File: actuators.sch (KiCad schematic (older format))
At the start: 16 parts

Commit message: Add digital outputs with NPN stage
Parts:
- added CONN? (x10): GPO, symbol GPO
- added Q? (x10): MBT3904DW1T1, SOT-363, symbol MBT3904DW1T1
- added R? (x10): 1k, symbol R_Small
- added R? (x10): 150, symbol R_Small
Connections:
- net labels added: OUT_1, OUT_10, OUT_2, OUT_3, OUT_4, OUT_5, OUT_6, OUT_7, OUT_8, OUT_9
- wire segments 28 -> 68
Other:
- note added: "150 ohm resistor limits NPN current to about 20mA"

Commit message: Annotate
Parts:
- gave numbers to parts that had none: 51

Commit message: Add connector for RGB LED
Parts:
- added CONN?: RGB, symbol RGB
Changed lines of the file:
@@
 Text Notes 1350 6150 0    60   ~ 0
 150 ohm resistor limits NPN current to about 20mA
+$Comp
+L RGB CONN?
+U 1 1 56BE642C
+P 10450 2325
+F 0 "CONN?" H 10627 2627 59  0000 L CNN
+F 1 "RGB" H 10627 2523 59  0000 L CNN
+F 2 "" H 10450 2325 59  0000 C CNN
+F 3 "" H 10450 2325 59  0000 C CNN
+	1    10450 2325
+	1    0    0    -1
+$EndComp
+Text Label 10100 1925 2    47   ~ 0
+RGB_LED_R
+Text Label 10100 2025 2    47   ~ 0
+RGB_LED_G
+Text Label 10100 2125 2    47   ~ 0
+RGB_LED_B
+$Comp
+L GND #PWR?
+U 1 1 56BE6827
+P 10100 2225
+F 0 "#PWR?" H 10100 1975 50  0001 C CNN
+F 1 "GND" H 10100 2075 50  0000 C CNN
+F 2 "" H 10100 2225 50  0000 C CNN
+F 3 "" H 10100 2225 50  0000 C CNN
+	1    10100 2225
+	1    0    0    -1
+$EndComp
 $EndSCHEMATC

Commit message: Correct digital outputs as we want to drive loads (LEDs)
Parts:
- removed CONN15, CONN16, CONN27, CONN28, CONN39, CONN40, CONN46, CONN47, CONN7, CONN8: GPO, symbol GPO
- added CONN15, CONN16, CONN27, CONN28, CONN39, CONN40, CONN46, CONN47, CONN7, CONN8: LOAD, symbol LOAD
- gave numbers to parts that had none: 1
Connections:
- wire segments 68 -> 77
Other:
- note added: "150 ohm resistor limits NPN current to \nabout 20mA if the load has no resistance"
- note removed: "150 ohm resistor limits NPN current to about 20mA"
- moved on the sheet: Q1B, Q2B, Q3B, Q4B, Q5B, R15, R2, R27, R3, R39, R49

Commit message: Fix small details & replot pdf
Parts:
- renumbered C1 to C17, CONN7 to CONN17, CONN8 to CONN18, CONN15 to CONN19, CONN16 to CONN20, CONN17 to CONN21, CONN18 to CONN22, CONN25 to CONN23, CONN26 to CONN24, CONN27 to CONN25, CONN28 to CONN26, CONN29 to CONN27, CONN30 to CONN28, CONN35 to CONN29, CONN36 to CONN30, CONN39 to CONN31, CONN40 to CONN32, CONN37 to CONN33, CONN38 to CONN34, CONN43 to CONN35, CONN44 to CONN36, CONN46 to CONN37, CONN47 to CONN38, CONN45 to CONN39, CONN54 to CONN40, R1 to R43, R2 to R44, R3 to R45, R4 to R46, R5 to R47, R14 to R48, R15 to R49, R16 to R50, R17 to R51, R26 to R52, R27 to R53, R28 to R54, R29 to R55, R38 to R56, R39 to R57, R44 to R58, R45 to R59, R48 to R60, R49 to R61, R50 to R62, R51 to R63, U1 to U6

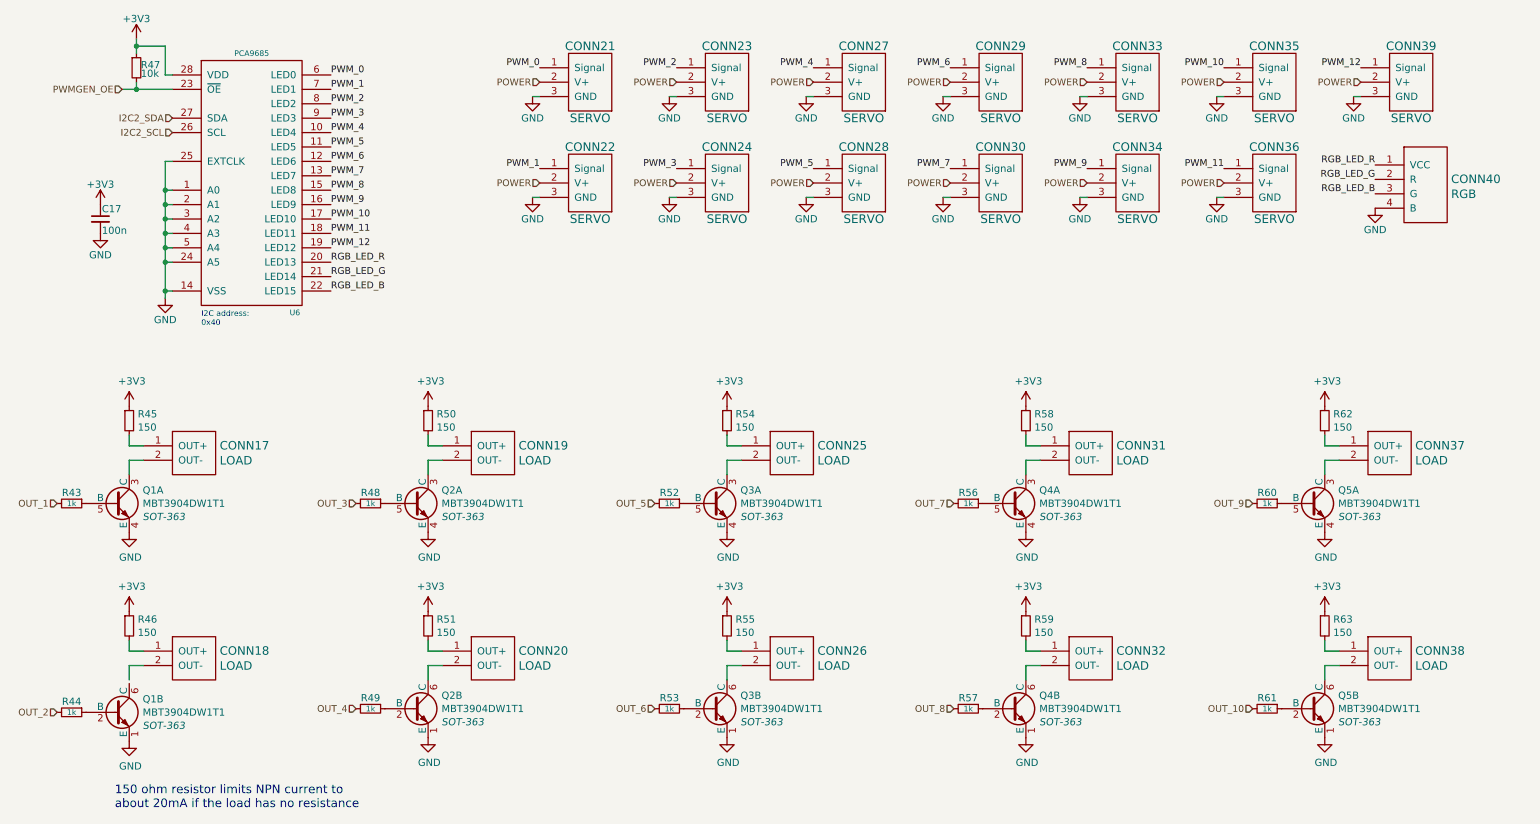
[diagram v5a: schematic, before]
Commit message: Correct schematic after review by @vieillemaison
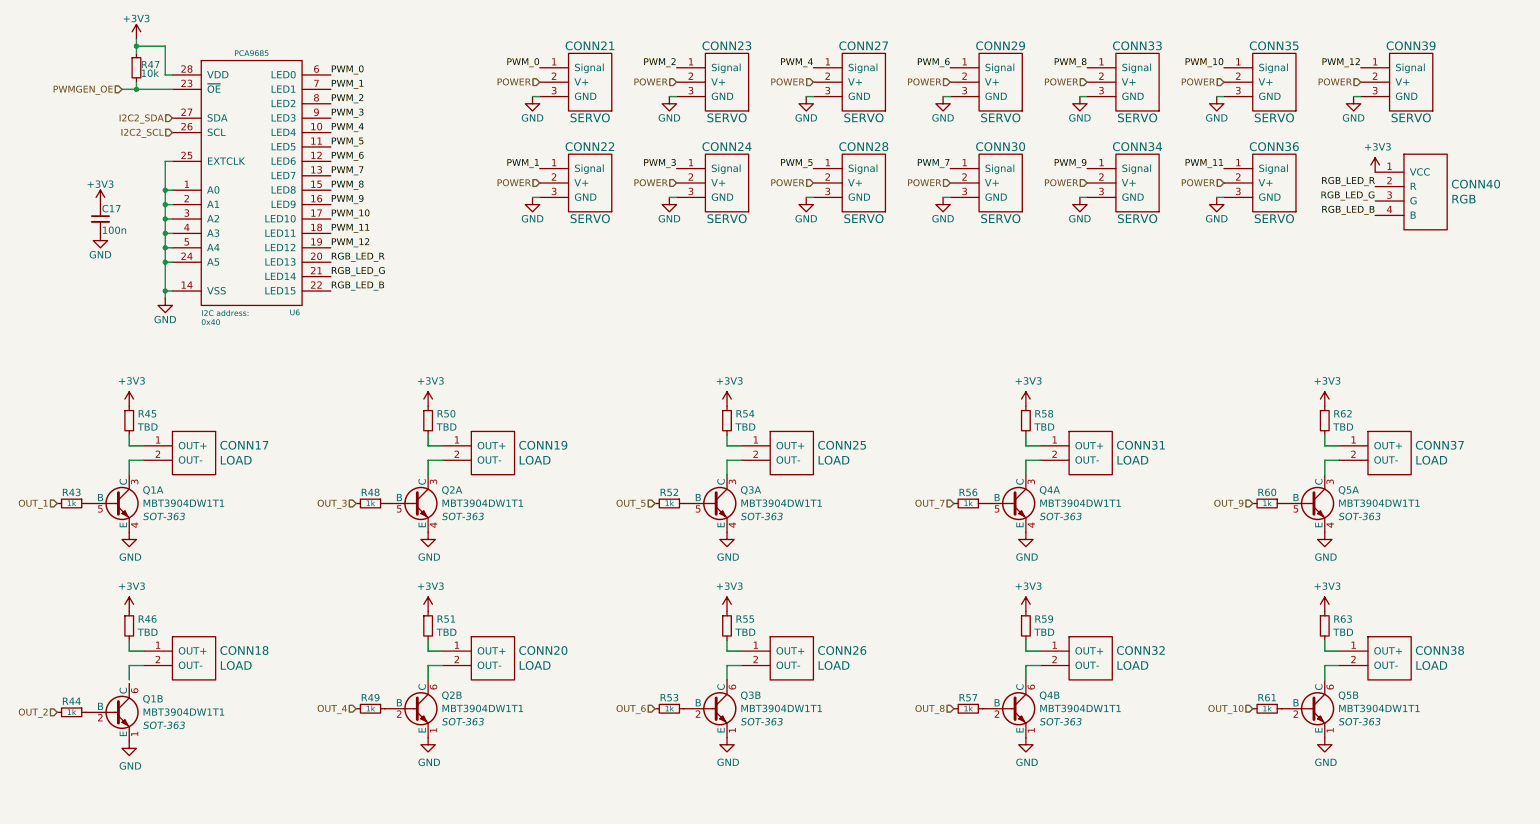
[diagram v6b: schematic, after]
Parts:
- R45, R46, R50, R51, R54, R55, R58, R59, R62, R63: value 150 -> TBD
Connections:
- net +3V3: now also CONN40.1 (VCC)
- net GND: no longer CONN40.4 (B)
- net RGB_LED_B: now also CONN40.4 (B); no longer CONN40.3 (G)
- net RGB_LED_G: now also CONN40.3 (G); no longer CONN40.2 (R)
- net RGB_LED_R: now also CONN40.2 (R); no longer CONN40.1 (VCC)
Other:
- note removed: "150 ohm resistor limits NPN current to \nabout 20mA if the load has no resistance"
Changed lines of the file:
@@
 P 1450 3700
 F 0 "R45" H 1509 3746 50  0000 L CNN
-F 1 "150" H 1509 3654 50  0000 L CNN
+F 1 "TBD" H 1509 3654 50  0000 L CNN
 F 2 "" H 1450 3700 50  0000 C CNN
 F 3 "" H 1450 3700 50  0000 C CNN
@@
 	1    0    0    -1
 $EndComp
-Text Notes 1350 6400 0    60   ~ 0
-150 ohm resistor limits NPN current to \nabout 20mA if the load has no resistance
-$Comp
-L RGB CONN40
-U 1 1 56BE642C
-P 10450 2325
-F 0 "CONN40" H 10627 2627 59  0000 L CNN
-F 1 "RGB" H 10627 2523 59  0000 L CNN
-F 2 "" H 10450 2325 59  0000 C CNN
-F 3 "" H 10450 2325 59  0000 C CNN
-	1    10450 2325
-	1    0    0    -1
-$EndComp
-Text Label 10100 1925 2    47   ~ 0
+Text Label 10100 2075 2    47   ~ 0
 RGB_LED_R
-Text Label 10100 2025 2    47   ~ 0
+Text Label 10100 2175 2    47   ~ 0
 RGB_LED_G
-Text Label 10100 2125 2    47   ~ 0
+Text Label 10100 2275 2    47   ~ 0
 RGB_LED_B
-$Comp
-L GND #PWR132
-U 1 1 56BE6827
-P 10100 2225
-F 0 "#PWR132" H 10100 1975 50  0001 C CNN
-F 1 "GND" H 10100 2075 50  0000 C CNN
-F 2 "" H 10100 2225 50  0000 C CNN
-F 3 "" H 10100 2225 50  0000 C CNN
-	1    10100 2225
-	1    0    0    -1
-$EndComp
 $Comp
 L LOAD CONN17
@@
 P 1450 5125
 F 0 "R46" H 1509 5171 50  0000 L CNN
-F 1 "150" H 1509 5079 50  0000 L CNN
+F 1 "TBD" H 1509 5079 50  0000 L CNN
 F 2 "" H 1450 5125 50  0000 C CNN
 F 3 "" H 1450 5125 50  0000 C CNN
@@
 P 3525 3700
 F 0 "R50" H 3584 3746 50  0000 L CNN
-F 1 "150" H 3584 3654 50  0000 L CNN
+F 1 "TBD" H 3584 3654 50  0000 L CNN
 F 2 "" H 3525 3700 50  0000 C CNN
 F 3 "" H 3525 3700 50  0000 C CNN
@@
 P 3525 5125
 F 0 "R51" H 3584 5171 50  0000 L CNN
-F 1 "150" H 3584 5079 50  0000 L CNN
+F 1 "TBD" H 3584 5079 50  0000 L CNN
 F 2 "" H 3525 5125 50  0000 C CNN
 F 3 "" H 3525 5125 50  0000 C CNN
@@
 P 5600 5125
 F 0 "R55" H 5659 5171 50  0000 L CNN
-F 1 "150" H 5659 5079 50  0000 L CNN
+F 1 "TBD" H 5659 5079 50  0000 L CNN
 F 2 "" H 5600 5125 50  0000 C CNN
 F 3 "" H 5600 5125 50  0000 C CNN
@@
 P 7675 5125
 F 0 "R59" H 7734 5171 50  0000 L CNN
-F 1 "150" H 7734 5079 50  0000 L CNN
+F 1 "TBD" H 7734 5079 50  0000 L CNN
 F 2 "" H 7675 5125 50  0000 C CNN
 F 3 "" H 7675 5125 50  0000 C CNN
@@
 P 5600 3700
 F 0 "R54" H 5659 3746 50  0000 L CNN
-F 1 "150" H 5659 3654 50  0000 L CNN
+F 1 "TBD" H 5659 3654 50  0000 L CNN
 F 2 "" H 5600 3700 50  0000 C CNN
 F 3 "" H 5600 3700 50  0000 C CNN
@@
 P 7675 3700
 F 0 "R58" H 7734 3746 50  0000 L CNN
-F 1 "150" H 7734 3654 50  0000 L CNN
+F 1 "TBD" H 7734 3654 50  0000 L CNN
 F 2 "" H 7675 3700 50  0000 C CNN
 F 3 "" H 7675 3700 50  0000 C CNN
@@
 P 9750 3700
 F 0 "R62" H 9809 3746 50  0000 L CNN
-F 1 "150" H 9809 3654 50  0000 L CNN
+F 1 "TBD" H 9809 3654 50  0000 L CNN
 F 2 "" H 9750 3700 50  0000 C CNN
 F 3 "" H 9750 3700 50  0000 C CNN
@@
 P 9750 5125
 F 0 "R63" H 9809 5171 50  0000 L CNN
-F 1 "150" H 9809 5079 50  0000 L CNN
+F 1 "TBD" H 9809 5079 50  0000 L CNN
 F 2 "" H 9750 5125 50  0000 C CNN
 F 3 "" H 9750 5125 50  0000 C CNN
@@
 Wire Wire Line
 	9750 5300 9850 5300
+$Comp
+L RGB CONN40
+U 1 1 56C8B91F
+P 10450 2375
+F 0 "CONN40" H 10628 2690 59  0000 L CNN
+F 1 "RGB" H 10628 2586 59  0000 L CNN
+F 2 "" H 10450 2375 59  0000 C CNN
+F 3 "" H 10450 2375 59  0000 C CNN
+	1    10450 2375
+	1    0    0    -1
+$EndComp
+$Comp
+L +3V3 #PWR?
+U 1 1 56C8BA87
+P 10100 1975
+F 0 "#PWR?" H 10100 1825 50  0001 C CNN
+F 1 "+3V3" H 10118 2149 50  0000 C CNN
+F 2 "" H 10100 1975 50  0000 C CNN
+F 3 "" H 10100 1975 50  0000 C CNN
+	1    10100 1975
+	1    0    0    -1
+$EndComp
 $EndSCHEMATC

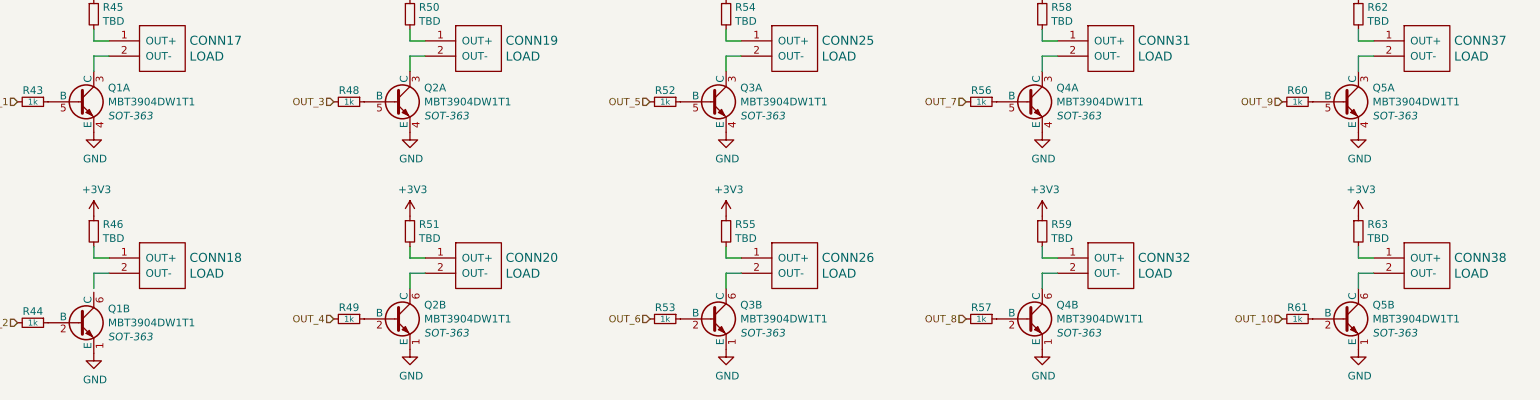
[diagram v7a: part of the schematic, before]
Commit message: Add a recharge circuit for the RTC backup battery
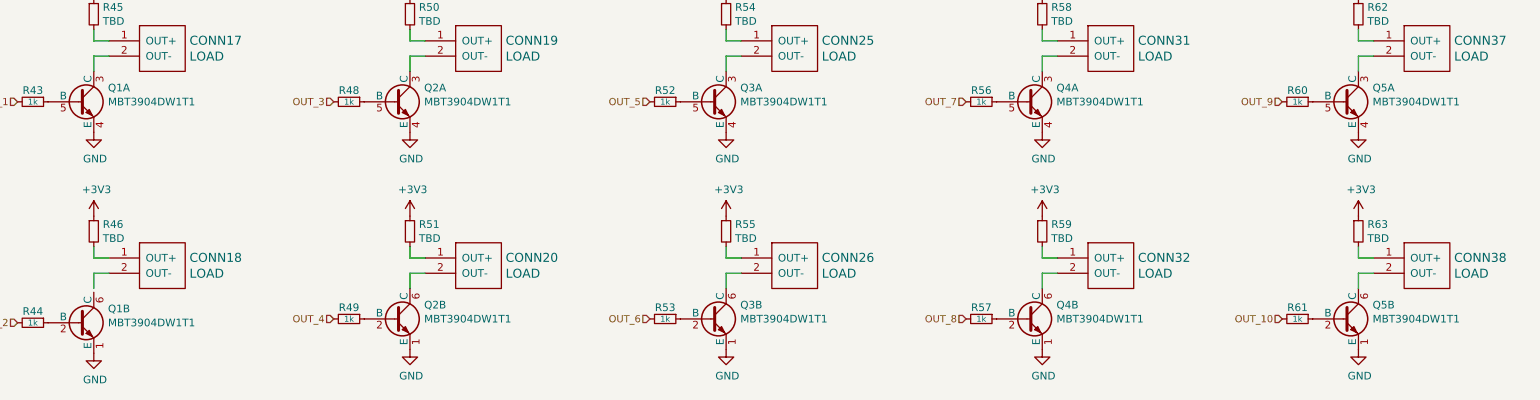
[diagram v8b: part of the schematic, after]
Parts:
- C17: footprint (none) -> _std:_0603
- Q1, Q2, Q3, Q4, Q5: footprint SOT-363 -> (none)
